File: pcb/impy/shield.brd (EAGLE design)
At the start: 133 x 107 mm, 117 parts, among them J1 USB-2410-06, J2 SI-60062-F, J3 5V, U1 AD5933YRS, U10 LTC3406AB, U11 23LCV1024-I/SN, U12 MIC2009A-1YM6, U13 ADG725BSU, U14 ADG725BSU, U2 ADG704BRM, U3 AD8656ARZ, U4 M24C08WMN, U5 ADG706BRU, U6 DP83848I, U7 MIC2009A-1YM6, U8 AT25DF081A-SS, U9 SST25VF080B-80-4I-S2

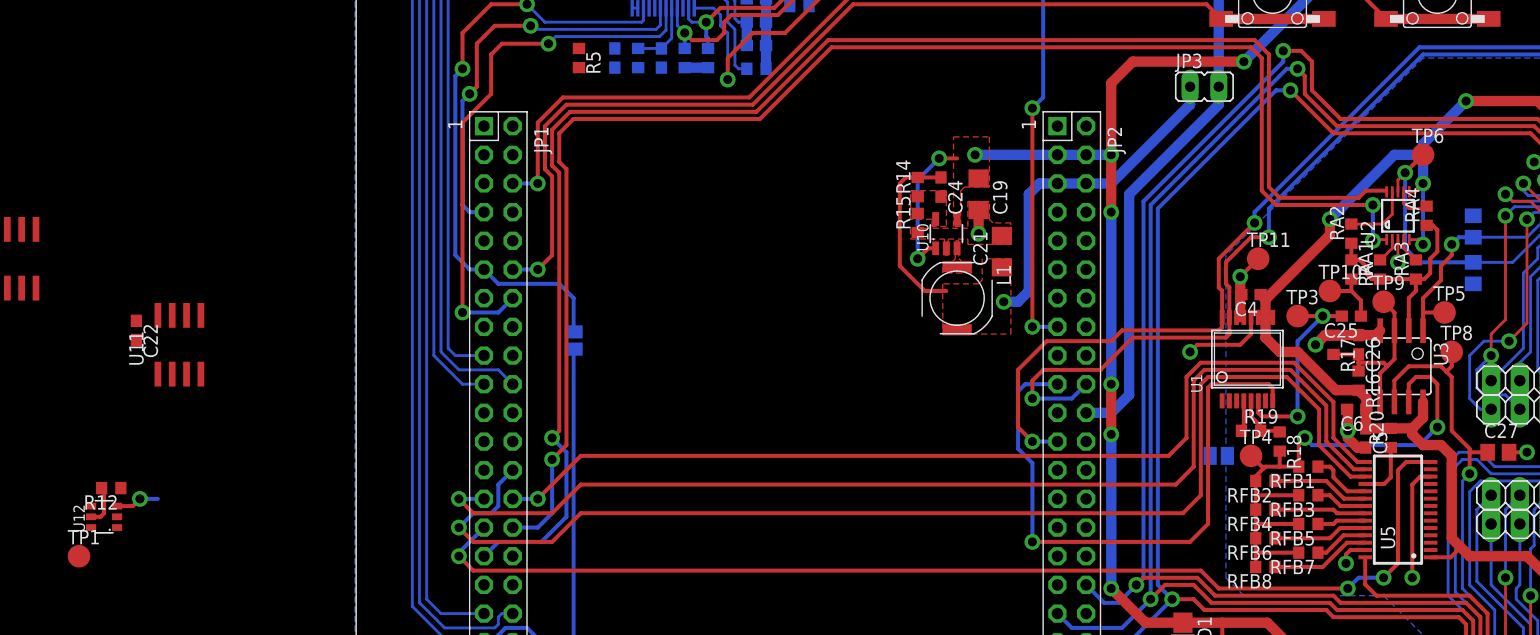
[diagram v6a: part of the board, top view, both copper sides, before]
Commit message: * pcb/impy: (shield.sch) Move Icc measurement jumper after switch for easier layout.
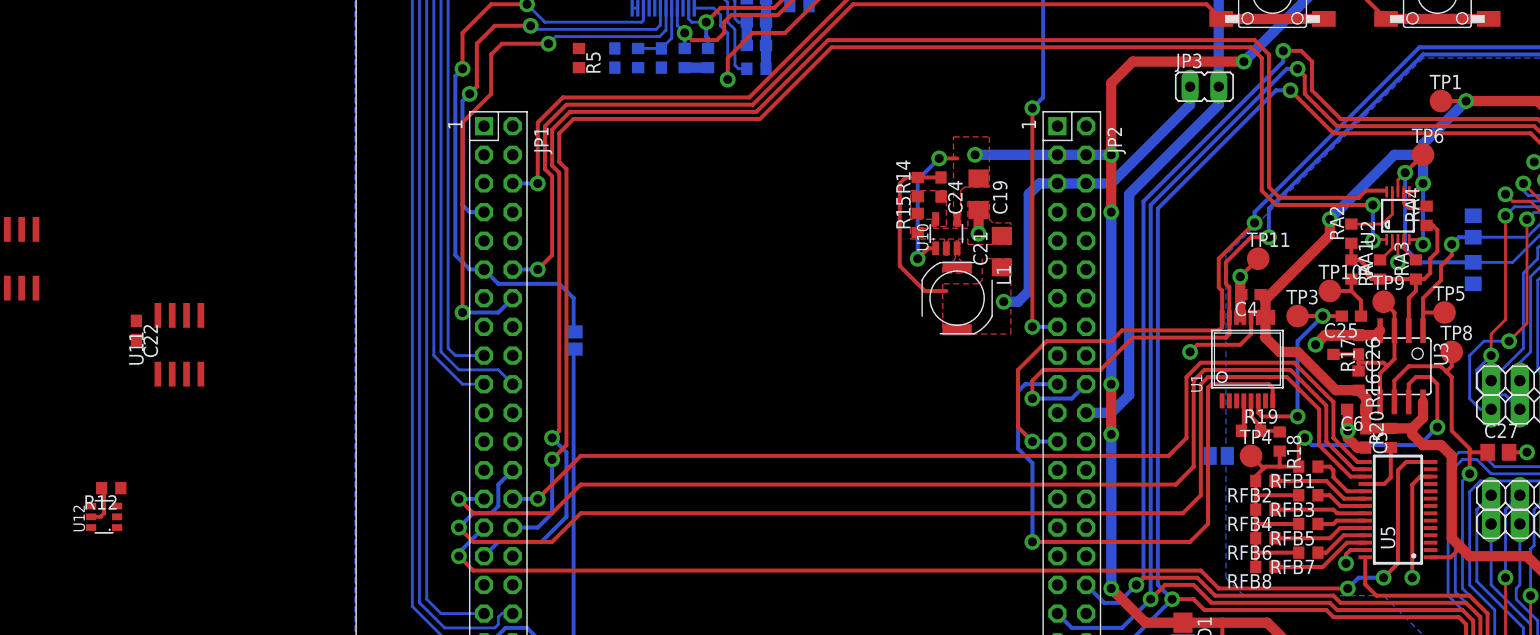
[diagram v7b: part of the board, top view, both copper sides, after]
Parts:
- moved TP1 127.2 mm to (58.1, 65.7)
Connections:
- net +3V3: now also U12.1; no longer JP4.2
- net N$36: now also JP4.2, U12.6; no longer JP4.1, U12.1
- net VCC: now also JP4.1; no longer U12.6
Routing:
- net PB10: track 3.88 -> 0.00 mm, vias 1 -> 0
- net VCC: track 193.7 -> 195.9 mm
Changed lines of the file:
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@@
 <element name="C29" library="rcl" package="C0805" value="N/A" x="60.96" y="54.61" rot="MR90"/>
 <element name="C30" library="rcl" package="C0805" value="N/A" x="60.96" y="50.4825" rot="MR90"/>
-<element name="TP1" library="testpad" package="TP20R" value="TPTP20R" x="-62.5475" y="25.4">
-<attribute name="TP_SIGNAL_NAME" value="VCC" x="-62.5475" y="25.4" size="1.778" layer="27" display="off"/>
+<element name="TP1" library="testpad" package="TP20R" value="TPTP20R" x="58.1025" y="65.7225">
+<attribute name="TP_SIGNAL_NAME" value="VCC" x="58.1025" y="65.7225" size="1.778" layer="27" display="off"/>
 </element>
 <element name="TP2" library="testpad" package="TP20R" value="TPTP20R" x="38.735" y="17.4625" rot="R180">
@@
 <contactref element="JP2" pad="6"/>
 <contactref element="JP3" pad="1"/>
-<contactref element="JP4" pad="2"/>
 <contactref element="C21" pad="1"/>
 <contactref element="R14" pad="2"/>
@@
 <wire x1="28.8925" y1="58.42" x2="35.8775" y2="65.405" width="0.9144" layer="16"/>
 <wire x1="35.8775" y1="65.405" x2="35.8775" y2="66.9925" width="0.9144" layer="16"/>
-<wire x1="10.16" y1="51.1175" x2="-53.0225" y2="11.43" width="0" layer="19" extent="1-1"/>
+<contactref element="U12" pad="1"/>
+<wire x1="10.16" y1="51.1175" x2="-59.175" y2="27.9425" width="0" layer="19" extent="1-1"/>
 </signal>
 <signal name="!RST">
@@
 <contactref element="RS3" pad="1"/>
 <contactref element="R11" pad="2"/>
-<contactref element="U12" pad="6"/>
 <contactref element="U3" pad="8"/>
 <contactref element="U2" pad="6"/>
@@
 <wire x1="56.515" y1="61.9125" x2="56.515" y2="60.96" width="0.9144" layer="16"/>
 <wire x1="56.515" y1="60.96" x2="56.515" y2="58.42" width="0.9144" layer="16"/>
+<wire x1="58.1025" y1="65.7225" x2="60.325" y2="65.7225" width="0.3556" layer="1"/>
+<contactref element="JP4" pad="1"/>
 <wire x1="79.0575" y1="91.1225" x2="88.2015" y2="91.4019" width="0" layer="19" extent="16-16"/>
 <wire x1="66.675" y1="65.7225" x2="71.755" y2="81.495" width="0" layer="19" extent="1-16"/>
@@
 <wire x1="-75.2475" y1="38.9925" x2="-76.5175" y2="44.1925" width="0" layer="19" extent="1-1"/>
 <wire x1="-75.2575" y1="38.4385" x2="-75.2475" y2="38.9925" width="0" layer="19" extent="1-1"/>
-<wire x1="-61.475" y1="27.9425" x2="-75.2575" y2="38.4385" width="0" layer="19" extent="1-1"/>
-<wire x1="-62.5475" y1="25.4" x2="-61.475" y2="27.9425" width="0" layer="19" extent="1-1"/>
+<wire x1="-53.0225" y1="13.97" x2="-57.4675" y2="46.2525" width="0" layer="19" extent="1-1"/>
 </signal>
 <signal name="AGND" class="1">
@@
 <wire x1="22.86" y1="66.04" x2="22.86" y2="84.1375" width="0.3556" layer="16"/>
 </signal>
-<signal name="N$36" class="1">
-<contactref element="U12" pad="1"/>
-<contactref element="JP4" pad="1"/>
-<wire x1="-59.175" y1="27.9425" x2="-53.0225" y2="13.97" width="0" layer="19" extent="1-1"/>
-</signal>
 <signal name="PB10">
 <contactref element="JP1" pad="34"/>
 <contactref element="U12" pad="3"/>
-<wire x1="-59.175" y1="29.8425" x2="-57.7875" y2="29.8425" width="0.3556" layer="1"/>
-<wire x1="-57.7875" y1="29.8425" x2="-57.15" y2="30.48" width="0.3556" layer="1"/>
-<via x="-57.15" y="30.48" extent="1-16" drill="0.8" shape="octagon"/>
-<wire x1="-57.15" y1="30.48" x2="-55.5625" y2="30.48" width="0.3556" layer="16"/>
-<wire x1="-24.13" y1="22.86" x2="-55.5625" y2="30.48" width="0" layer="19" extent="16-16"/>
+<wire x1="-24.13" y1="22.86" x2="-59.175" y2="29.8425" width="0" layer="19" extent="1-1"/>
 </signal>
 <signal name="N$37">
@@
 <wire x1="69.7475" y1="79.375" x2="69.85" y2="79.375" width="0.3556" layer="1"/>
 </signal>
+<signal name="N$36">
+<contactref element="U12" pad="6"/>
+<contactref element="JP4" pad="2"/>
+<wire x1="-61.475" y1="27.9425" x2="-53.0225" y2="11.43" width="0" layer="19" extent="1-1"/>
+</signal>
 </signals>

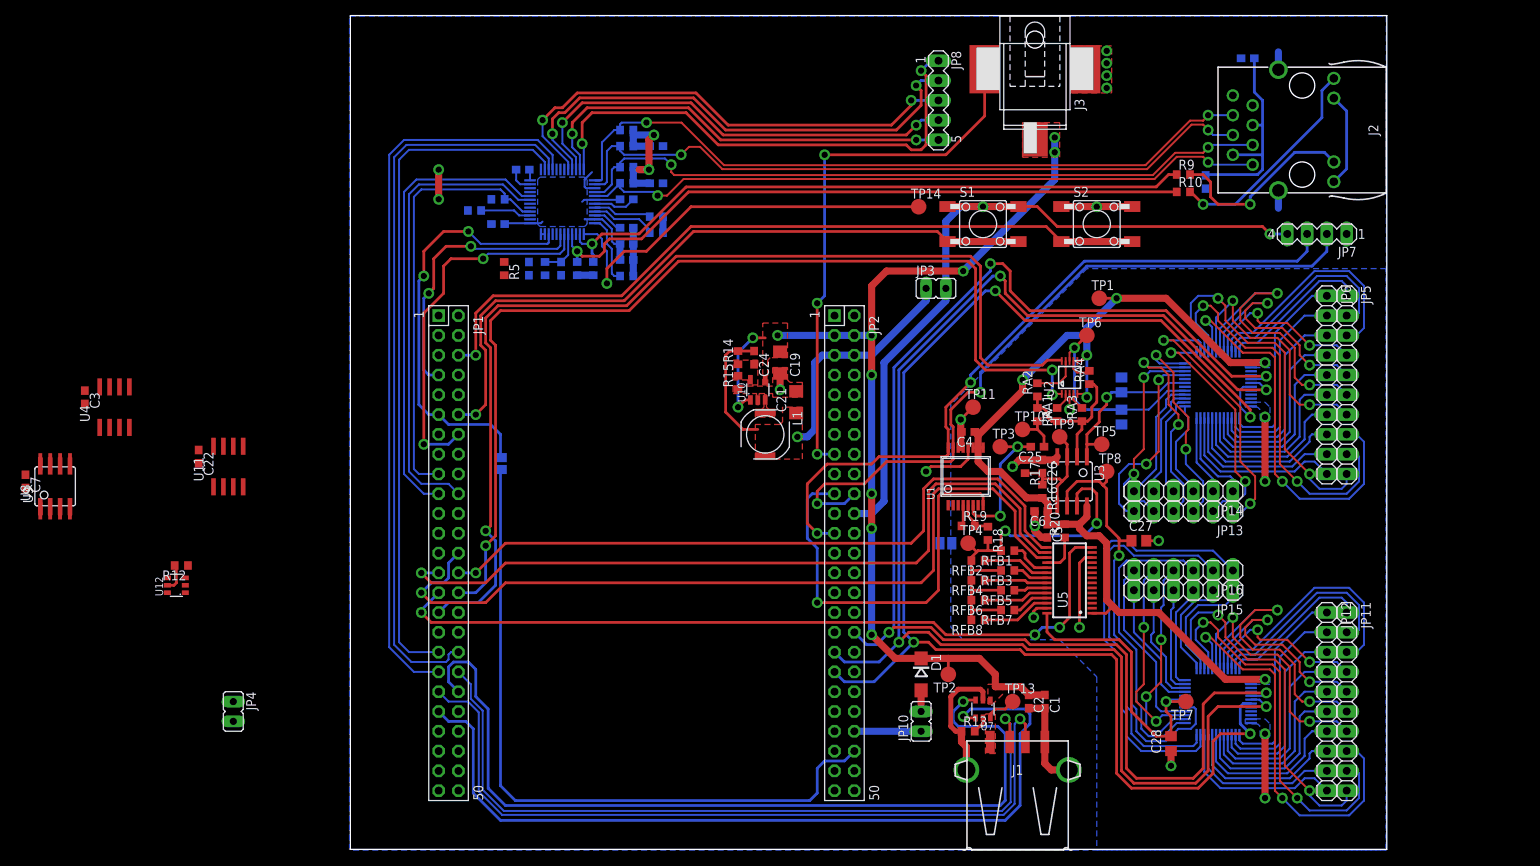
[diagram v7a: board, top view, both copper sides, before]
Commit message: * pcb/impy: (shield.brd) Place and route SPI memories. Move main power switch near switching regulator.
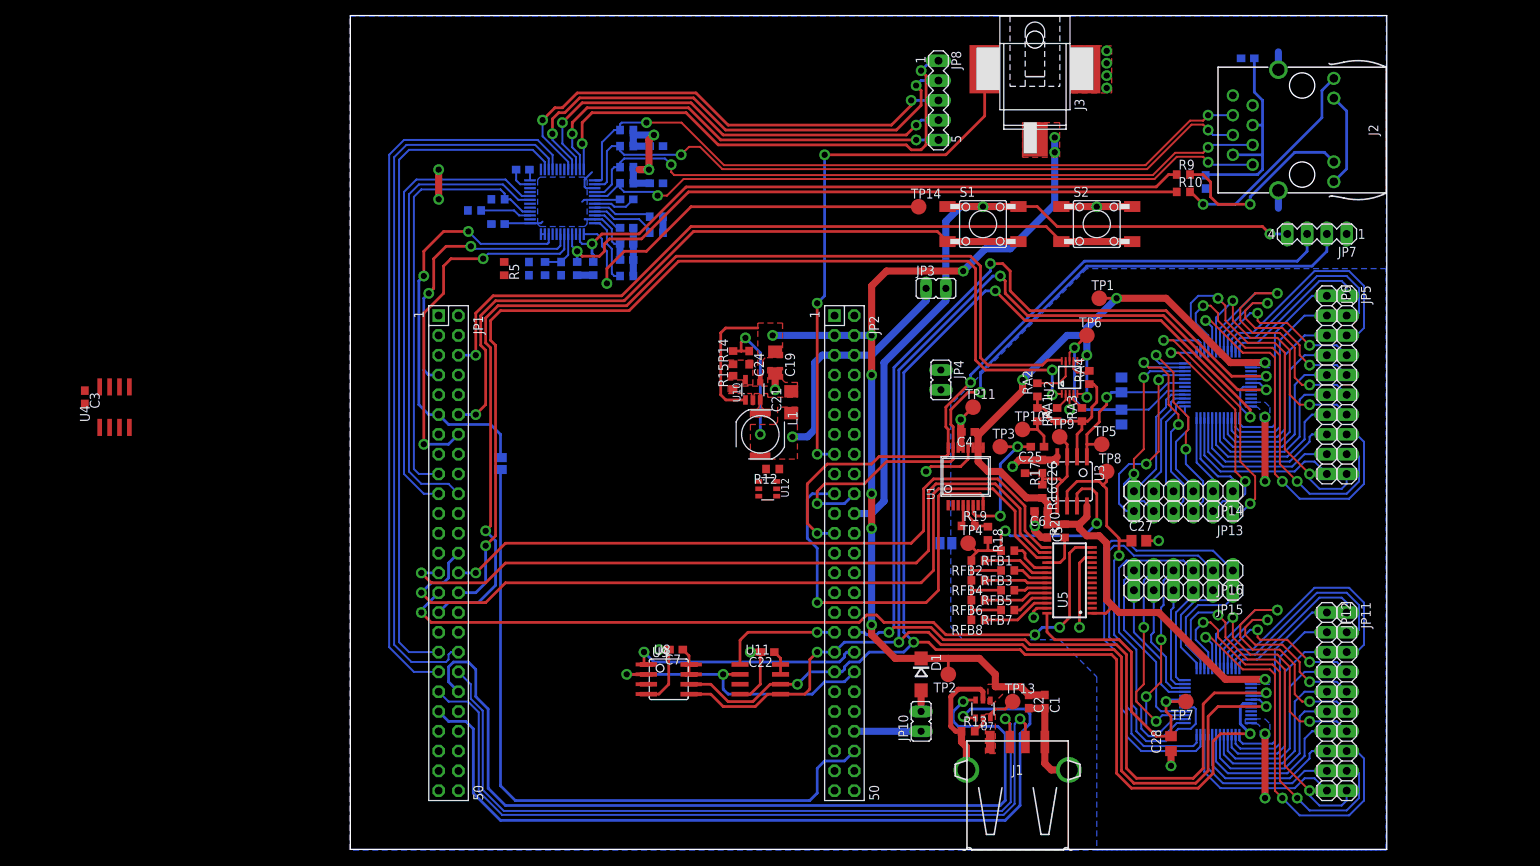
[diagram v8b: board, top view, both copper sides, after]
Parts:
- moved JP4 100.3 mm to (37.8, 55.2)
- moved C7 86.2 mm to (3.81, 20.6), turned to 180 degrees
- moved U8 82.5 mm to (2.86, 16.8), turned to 270 degrees
- moved U9 82.5 mm to (2.86, 16.8), turned to 270 degrees
- moved C22 77.2 mm to (15.6, 20.3), turned to 180 degrees
- moved U12 76.9 mm to (15.6, 41.3), turned to 270 degrees
- moved R12 76.9 mm to (16.2, 43.8)
- moved U11 73.5 mm to (14.6, 16.8), turned to 270 degrees
- moved C24 0.63 mm to (13.2, 58.1)
- moved L1 0.63 mm to (14.6, 48.3)
- moved R14 0.63 mm to (11.1, 58.1)
- moved R15 0.63 mm to (11.1, 54.9)
- moved U10 0.63 mm to (13.7, 54.0)
- moved C19 0.63 mm to (16.5, 57.5)
- moved C21 0.63 mm to (18.6, 52.4)
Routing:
- net PC11: track 0.00 -> 37.5 mm, vias 0 -> 2
- net PD0: track 0.00 -> 30.4 mm, vias 0 -> 1
- net PC12: track 180.9 -> 204.3 mm, vias 4 -> 5
- net PC10: track 179.9 -> 200.2 mm, vias 4 -> 5
- net GND: track 75.3 -> 93.5 mm, vias 9 -> 11
- net PD1: track 0.00 -> 15.7 mm, vias 0 -> 1
- net VCC: track 195.9 -> 204.3 mm
- net +5V: track 133.0 -> 138.7 mm, vias 11 -> 9
- net N$38: track 3.59 -> 0.00 mm
- net +3V3: track 46.6 -> 48.1 mm, vias 1 -> 3
- net PD2: track 180.1 -> 179.1 mm
- net PE11: track 100.2 -> 101.0 mm
